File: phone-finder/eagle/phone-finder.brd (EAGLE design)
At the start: 50 x 50 mm, 45 parts, among them J1 MICRO USB, J2 PHONE-JACK, K1 RELAY, Q1 DTA114EET1G (2x10K), Q2 2N2222, Q3 2N2222, T1 TRANSFORMER, U1 AP2114H-3.3TRG1, U2 NUF2042XV6T1G, U3 LPC11U35FHI33/501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

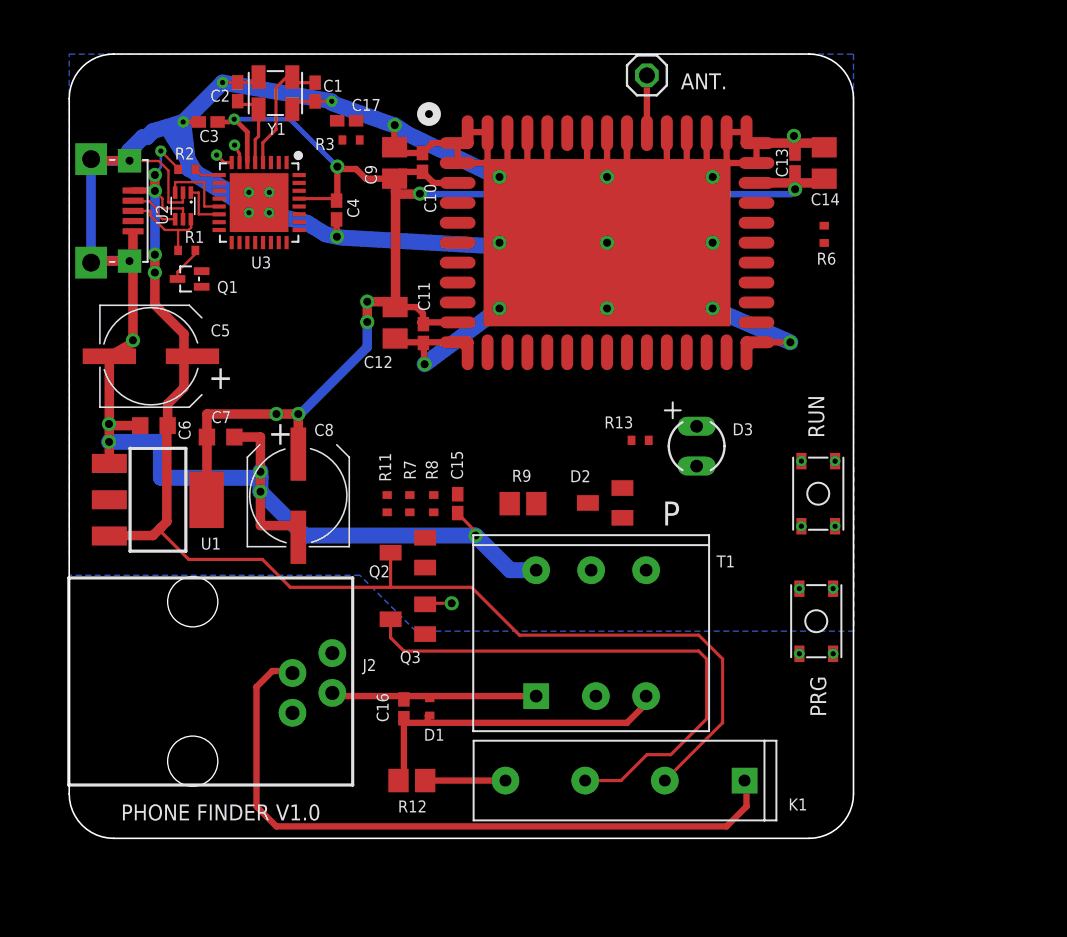
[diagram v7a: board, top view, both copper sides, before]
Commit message: Fixed phone jack footprint.
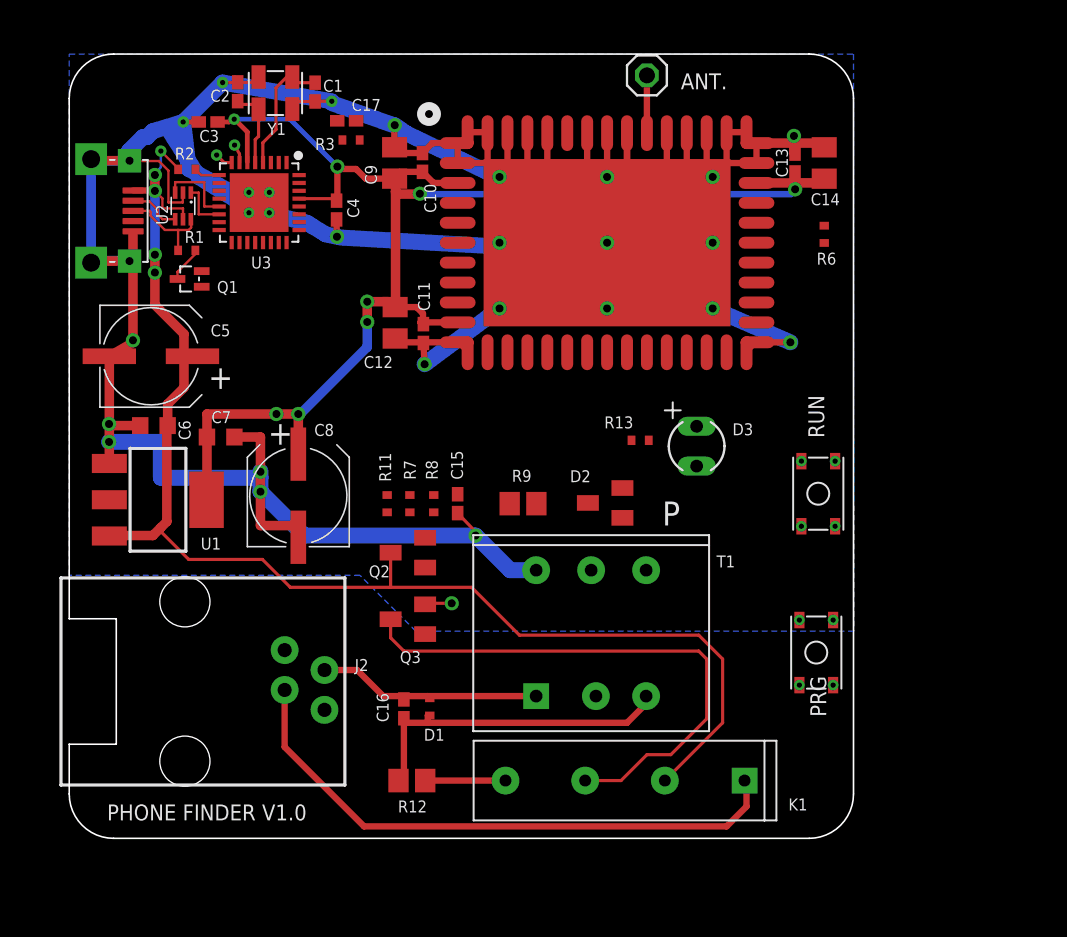
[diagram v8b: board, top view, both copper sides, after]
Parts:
- moved S1 2.00 mm to (47.6, 11.8)
- moved J2 0.50 mm to (7.37, 10.0)
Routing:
- net N$11: track 44.2 -> 37.4 mm
- net N$10: track 13.6 -> 14.7 mm
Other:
- outline, holes or cut-outs redrawn
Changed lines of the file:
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@@
 <setting verticaltext="up"/>
 </settings>
-<grid distance="5" unitdist="mil" unit="mil" style="lines" multiple="1" display="no" altdistance="1" altunitdist="mil" altunit="mil"/>
+<grid distance="5" unitdist="mil" unit="mm" style="lines" multiple="1" display="no" altdistance="1" altunitdist="mil" altunit="mil"/>
 <layers>
 <layer number="1" name="Top" color="4" fill="1" visible="yes" active="yes"/>
@@
 <wire x1="47.171575" y1="50" x2="2.828425" y2="50" width="0.1016" layer="20"/>
 <wire x1="2.828425" y1="50" x2="0" y2="47.171575" width="0.1016" layer="20" curve="90"/>
-<wire x1="0" y1="47.171575" x2="0" y2="2.828425" width="0.1016" layer="20"/>
+<wire x1="0" y1="47.171575" x2="0" y2="14" width="0.1016" layer="20"/>
+<wire x1="0" y1="14" x2="3" y2="14" width="0.1016" layer="20"/>
+<wire x1="3" y1="14" x2="3" y2="6" width="0.1016" layer="20"/>
+<wire x1="3" y1="6" x2="0" y2="6" width="0.1016" layer="20"/>
+<wire x1="0" y1="6" x2="0" y2="2.828425" width="0.1016" layer="20"/>
 <wire x1="0" y1="2.828425" x2="2.828425" y2="0" width="0.1016" layer="20" curve="90"/>
 <wire x1="2.828425" y1="0" x2="47.171575" y2="0" width="0.1016" layer="20"/>
@@
 <wire x1="14.224" y1="14.605" x2="17.653" y2="14.605" width="0.2032" layer="41"/>
 <wire x1="17.653" y1="14.605" x2="21.336" y2="10.922" width="0.2032" layer="41"/>
-<wire x1="21.336" y1="10.922" x2="52.324" y2="10.922" width="0.2032" layer="41"/>
+<wire x1="21.336" y1="10.922" x2="42.672" y2="10.922" width="0.2032" layer="41"/>
+<wire x1="42.672" y1="10.922" x2="45.72" y2="7.366" width="0.2032" layer="41"/>
+<wire x1="45.72" y1="7.366" x2="53.594" y2="7.239" width="0.2032" layer="41"/>
 <wire x1="-1.524" y1="17.018" x2="11.811" y2="17.018" width="0.2032" layer="42"/>
 <wire x1="11.811" y1="17.018" x2="14.097" y2="14.732" width="0.2032" layer="42"/>
 <wire x1="14.097" y1="14.732" x2="17.653" y2="14.732" width="0.2032" layer="42"/>
 <wire x1="17.653" y1="14.732" x2="21.336" y2="10.922" width="0.2032" layer="42"/>
-<wire x1="21.336" y1="10.922" x2="53.213" y2="10.922" width="0.2032" layer="42"/>
+<wire x1="21.336" y1="10.922" x2="42.545" y2="10.922" width="0.2032" layer="42"/>
+<wire x1="42.545" y1="10.922" x2="45.593" y2="7.366" width="0.2032" layer="42"/>
+<wire x1="45.593" y1="7.366" x2="53.086" y2="7.366" width="0.2032" layer="42"/>
 <text x="8.8646" y="28.6512" size="1.524" layer="21" font="vector" ratio="10">+</text>
 <text x="38.989" y="47.752" size="1.016" layer="21" font="vector" ratio="10">ANT.</text>
-<text x="3.302" y="1.143" size="1.016" layer="21" font="vector" ratio="10">PHONE FINDER V1.0</text>
+<text x="2.413" y="1.143" size="1.016" layer="21" font="vector" ratio="10">PHONE FINDER V1.0</text>
 </plain>
 <attributes>
@@
 <elements>
 <element name="J1" library="phone-finder" package="USB-MICRO" value="MICRO USB" x="1.397" y="40" smashed="yes" rot="R270"/>
-<element name="S1" library="phone-finder" package="PUSH_BUTTON" value="PUSH-BUTTON" x="47.625" y="13.843" smashed="yes" rot="R270"/>
+<element name="S1" library="phone-finder" package="PUSH_BUTTON" value="PUSH-BUTTON" x="47.625" y="11.843" smashed="yes" rot="R270"/>
 <element name="C7" library="phone-finder" package="C0603K" value="1u" x="9.656" y="25.583" smashed="yes">
 <attribute name="NAME" x="10.321" y="27.234" size="0.762" layer="25" font="vector" ratio="10" rot="R180"/>
@@
 <attribute name="NAME" x="19.1008" y="16.637" size="0.762" layer="25" font="vector" ratio="10"/>
 </element>
-<element name="J2" library="phone-finder" package="PHONE-JACK" value="PHONE-JACK" x="7.874" y="10" smashed="yes" rot="R270">
-<attribute name="OC_NEWARK" value="unknown" x="7.874" y="10" size="1.778" layer="27" rot="R270" display="off"/>
-<attribute name="MPN" value="" x="7.874" y="10" size="1.778" layer="27" rot="R270" display="off"/>
-<attribute name="MF" value="" x="7.874" y="10" size="1.778" layer="27" rot="R270" display="off"/>
-<attribute name="OC_FARNELL" value="unknown" x="7.874" y="10" size="1.778" layer="27" rot="R270" display="off"/>
-<attribute name="NAME" x="18.702" y="10.668" size="0.762" layer="25" font="vector" ratio="10"/>
+<element name="J2" library="phone-finder" package="PHONE-JACK" value="PHONE-JACK" x="7.374" y="10" smashed="yes" rot="R270">
+<attribute name="OC_NEWARK" value="unknown" x="7.374" y="10" size="1.778" layer="27" rot="R270" display="off"/>
+<attribute name="MPN" value="" x="7.374" y="10" size="1.778" layer="27" rot="R270" display="off"/>
+<attribute name="MF" value="" x="7.374" y="10" size="1.778" layer="27" rot="R270" display="off"/>
+<attribute name="OC_FARNELL" value="unknown" x="7.374" y="10" size="1.778" layer="27" rot="R270" display="off"/>
+<attribute name="NAME" x="18.202" y="10.668" size="0.762" layer="25" font="vector" ratio="10"/>
 </element>
 <element name="D3" library="phone-finder" package="LED" value="LED" x="40" y="25" smashed="yes" rot="R270">
@@
 <contactref element="S1" pad="B2"/>
 <contactref element="S1" pad="B2P"/>
-<wire x1="46.55" y1="11.768" x2="46.55" y2="15.918" width="0" layer="19" extent="1-1"/>
-<wire x1="33.0668" y1="21.382" x2="46.55" y2="15.918" width="0" layer="19" extent="1-1"/>
+<wire x1="46.55" y1="9.768" x2="46.55" y2="13.918" width="0" layer="19" extent="1-1"/>
+<wire x1="33.0668" y1="21.382" x2="46.55" y2="13.918" width="0" layer="19" extent="1-1"/>
 </signal>
 <signal name="WIFI_RESET">
@@
 <contactref element="U3" pad="21"/>
 <contactref element="R6" pad="2"/>
-<wire x1="43.815" y1="40.513" x2="48.133" y2="37.9564" width="0" layer="19" extent="1-1"/>
+<wire x1="48.133" y1="37.9564" x2="43.815" y2="40.513" width="0" layer="19" extent="1-1"/>
 <wire x1="12.357" y1="37.982" x2="43.815" y2="40.513" width="0" layer="19" extent="1-1"/>
 </signal>
@@
 <wire x1="14.605" y1="19.194" x2="14.986" y2="19.304" width="0" layer="19" extent="1-16"/>
 <wire x1="12.107" y1="40.532" x2="11.938" y2="39.878" width="0" layer="19" extent="1-16"/>
-<wire x1="48.7" y1="11.768" x2="48.7" y2="15.918" width="0" layer="19" extent="1-1"/>
+<wire x1="48.7" y1="9.768" x2="48.7" y2="13.918" width="0" layer="19" extent="1-1"/>
 </signal>
 <signal name="N$13">
@@
 <contactref element="C16" pad="2"/>
 <contactref element="J2" pad="3"/>
-<wire x1="16.774" y1="9.27" x2="16.9762" y2="9.0678" width="0.4064" layer="1"/>
-<wire x1="16.9762" y1="9.0678" x2="21.5488" y2="9.0678" width="0.4064" layer="1"/>
-<wire x1="21.59" y1="9.0678" x2="22.86" y2="9.0678" width="0.4064" layer="1"/>
+<wire x1="21.5488" y1="9.0678" x2="22.86" y2="9.0678" width="0.4064" layer="1"/>
 <wire x1="22.86" y1="9.0678" x2="29.7688" y2="9.0678" width="0.4064" layer="1"/>
 <wire x1="22.987" y1="8.932" x2="22.86" y2="9.059" width="0.4064" layer="1"/>
 <wire x1="22.86" y1="9.059" x2="22.86" y2="9.0678" width="0.4064" layer="1"/>
 <wire x1="21.336" y1="8.855" x2="21.5488" y2="9.0678" width="0.4064" layer="1"/>
-<wire x1="21.5488" y1="9.0678" x2="21.59" y2="9.0678" width="0.4064" layer="1"/>
+<wire x1="16.274" y1="10.73" x2="18.353" y2="10.73" width="0.4064" layer="1"/>
+<wire x1="18.353" y1="10.73" x2="20.0152" y2="9.0678" width="0.4064" layer="1"/>
+<wire x1="20.0152" y1="9.0678" x2="21.5488" y2="9.0678" width="0.4064" layer="1"/>
 </signal>
 <signal name="DTMF1">
@@
 <signal name="N$11">
 <contactref element="J2" pad="4"/>
-<wire x1="11.938" y1="2.032" x2="13.208" y2="0.762" width="0.4064" layer="1"/>
 <contactref element="K1" pad="1"/>
 <wire x1="43.053" y1="3.683" x2="43.18" y2="3.556" width="0.4064" layer="1"/>
 <wire x1="43.18" y1="3.556" x2="43.18" y2="2.032" width="0.4064" layer="1"/>
 <wire x1="43.18" y1="2.032" x2="41.91" y2="0.762" width="0.4064" layer="1"/>
-<wire x1="41.91" y1="0.762" x2="13.208" y2="0.762" width="0.4064" layer="1"/>
-<wire x1="14.106" y1="10.668" x2="12.954" y2="10.668" width="0.4064" layer="1"/>
-<wire x1="12.954" y1="10.668" x2="11.938" y2="9.652" width="0.4064" layer="1"/>
-<wire x1="11.938" y1="9.652" x2="11.938" y2="2.032" width="0.4064" layer="1"/>
-<wire x1="14.106" y1="10.668" x2="14.234" y2="10.54" width="0" layer="19" extent="1-1"/>
+<wire x1="41.91" y1="0.762" x2="18.796" y2="0.762" width="0.4064" layer="1"/>
+<wire x1="18.796" y1="0.762" x2="13.734" y2="5.824" width="0.4064" layer="1"/>
+<wire x1="13.734" y1="5.824" x2="13.734" y2="9.46" width="0.4064" layer="1"/>
 </signal>
 <signal name="N$9">
